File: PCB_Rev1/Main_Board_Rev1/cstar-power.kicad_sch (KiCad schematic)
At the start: 49 parts, among them IC1 LT8648SEV#PBF, J4 Conn_01x02_Pin, J5 XT60PW-M, J6 Conn_01x02_Pin, J7 Conn_01x02_Pin, J8 Conn_01x02_Pin, U1 AZ1117IH-3.3TRG1

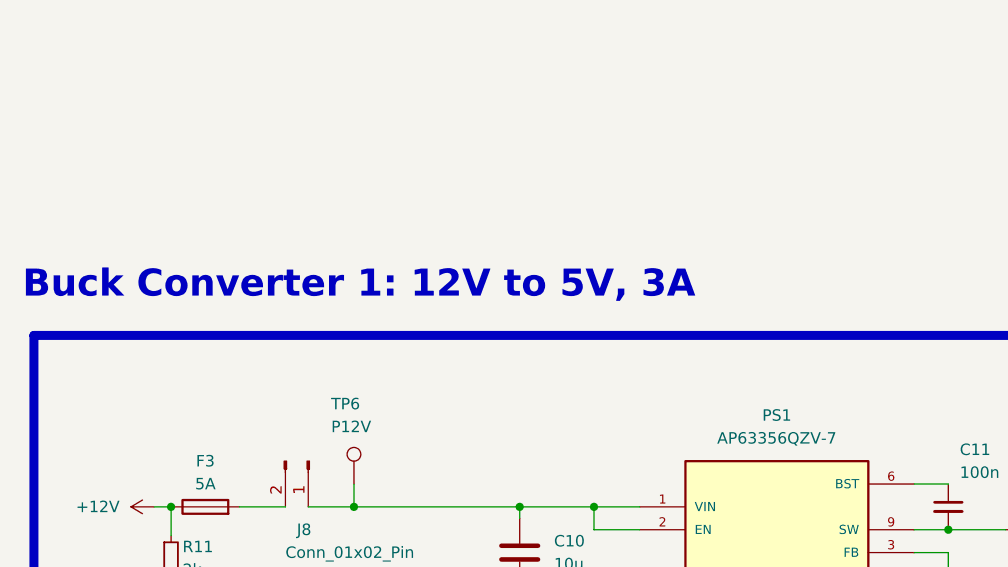
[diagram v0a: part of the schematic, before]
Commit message: LDO footprint assigned
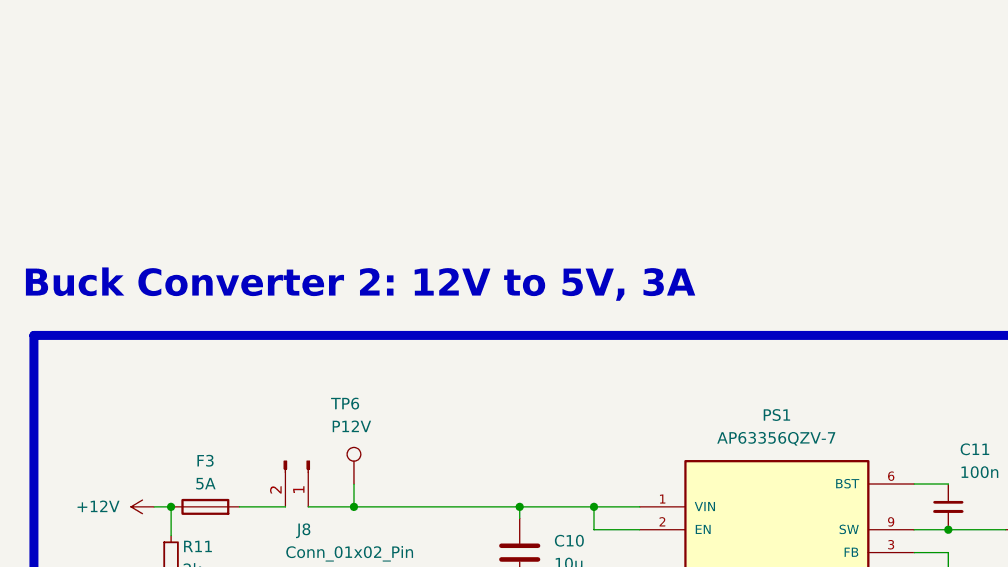
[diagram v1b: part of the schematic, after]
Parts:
- U1: footprint CSTAR-MainBoard-Footprints:SOT230P700X185-4N -> Footprints:LDO
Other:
- note added: "Buck Converter 2: 12V to 5V, 3A"
- note removed: "Buck Converter 1: 12V to 5V, 3A"
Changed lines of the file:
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@@
 		)
 	)
-	(text "Buck Converter 1: 12V to 5V, 3A\n"
+	(text "Buck Converter 2: 12V to 5V, 3A\n"
 		(exclude_from_sim no)
 		(at 43.18 191.77 0)
@@
 			)
 		)
-		(property "Footprint" "CSTAR-MainBoard-Footprints:SOT230P700X185-4N"
+		(property "Footprint" "Footprints:LDO"
 			(at 95.885 287.02 0)
 			(effects

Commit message: All BMS footprints added
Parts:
- IC1: footprint CSTAR-MainBoard-Footprints:Buck-05-08-1604_ADI -> Footprints:Buck_1
- PS1: footprint CSTAR-MainBoard-Footprints:IC9_AP63356QZV-7_DIO -> Footprints:Buck_2
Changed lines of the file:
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@@
 			)
 		)
-		(property "Footprint" "CSTAR-MainBoard-Footprints:IC9_AP63356QZV-7_DIO"
+		(property "Footprint" "Footprints:Buck_2"
 			(at 127 222.25 0)
 			(effects
@@
 			)
 		)
-		(property "Footprint" "CSTAR-MainBoard-Footprints:Buck-05-08-1604_ADI"
+		(property "Footprint" "Footprints:Buck_1"
 			(at 186.69 164.77 0)
 			(effects

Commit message: Added new footprints
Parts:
- LED1, LED2, LED3, LED4: footprint CSTAR-MainBoard-Footprints:LED_0VS75000_WRE -> (none)
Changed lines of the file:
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@@
 			)
 		)
-		(property "Footprint" "CSTAR-MainBoard-Footprints:LED_0VS75000_WRE"
+		(property "Footprint" ""
 			(at 170.18 316.23 0)
 			(effects
@@
 			)
 		)
-		(property "Footprint" "CSTAR-MainBoard-Footprints:LED_0VS75000_WRE"
+		(property "Footprint" ""
 			(at 58.42 316.865 0)
 			(effects
@@
 			)
 		)
-		(property "Footprint" "CSTAR-MainBoard-Footprints:LED_0VS75000_WRE"
+		(property "Footprint" ""
 			(at 91.44 80.01 0)
 			(effects
@@
 			)
 		)
-		(property "Footprint" "CSTAR-MainBoard-Footprints:LED_0VS75000_WRE"
+		(property "Footprint" ""
 			(at 59.69 225.425 0)
 			(effects

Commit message: more footprints changes
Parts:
- L1: footprint CSTAR-MainBoard-Footprints:L1_2.2uH -> (none)
- L2: footprint CSTAR-MainBoard-Footprints:L2_6.8uH -> (none)
- LED1, LED2, LED3, LED4: footprint (none) -> Footprints:LED_0VS75000_WRE
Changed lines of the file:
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@@
 			)
 		)
-		(property "Footprint" ""
+		(property "Footprint" "Footprints:LED_0VS75000_WRE"
 			(at 170.18 316.23 0)
 			(effects
@@
 			)
 		)
-		(property "Footprint" "CSTAR-MainBoard-Footprints:L1_2.2uH"
+		(property "Footprint" ""
 			(at 201.93 92.71 0)
 			(effects
@@
 			)
 		)
-		(property "Footprint" "CSTAR-MainBoard-Footprints:L2_6.8uH"
+		(property "Footprint" ""
 			(at 156.21 217.17 0)
 			(effects
@@
 			)
 		)
-		(property "Footprint" ""
+		(property "Footprint" "Footprints:LED_0VS75000_WRE"
 			(at 58.42 316.865 0)
 			(effects
@@
 			)
 		)
-		(property "Footprint" ""
+		(property "Footprint" "Footprints:LED_0VS75000_WRE"
 			(at 91.44 80.01 0)
 			(effects
@@
 			)
 		)
-		(property "Footprint" ""
+		(property "Footprint" "Footprints:LED_0VS75000_WRE"
 			(at 59.69 225.425 0)
 			(effects

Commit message: more footprints assigned
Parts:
- L1, L2: footprint (none) -> Inductor_SMD:L_0805_2012Metric
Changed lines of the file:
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@@
 			)
 		)
-		(property "Footprint" ""
+		(property "Footprint" "Inductor_SMD:L_0805_2012Metric"
 			(at 201.93 92.71 0)
 			(effects
@@
 			)
 		)
-		(property "Footprint" ""
+		(property "Footprint" "Inductor_SMD:L_0805_2012Metric"
 			(at 156.21 217.17 0)
 			(effects

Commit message: FOOTPRINTS COMPLETE!!!!!
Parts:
- D1: footprint CSTAR-MainBoard-Footprints:SMCJSeries_LTF -> Footprints:D1_Bi-dir
- J5: footprint CSTAR-MainBoard-Footprints:AMASS_XT60PW-M -> Connector_AMASS:AMASS_XT60PW-M_1x02_P7.20mm_Horizontal
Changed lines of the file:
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@@
 			)
 		)
-		(property "Footprint" "CSTAR-MainBoard-Footprints:AMASS_XT60PW-M"
+		(property "Footprint" "Connector_AMASS:AMASS_XT60PW-M_1x02_P7.20mm_Horizontal"
 			(at 363.22 336.55 0)
 			(effects
@@
 			)
 		)
-		(property "Footprint" "CSTAR-MainBoard-Footprints:SMCJSeries_LTF"
+		(property "Footprint" "Footprints:D1_Bi-dir"
 			(at 80.01 77.47 0)
 			(effects
